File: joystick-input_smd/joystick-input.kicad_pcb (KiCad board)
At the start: 2 copper layers, 53.3 x 38.6 mm, 16 parts, among them J1 Conn_01x18_Male, J2 Conn_01x14_Male, J3 Conn_01x14_Male

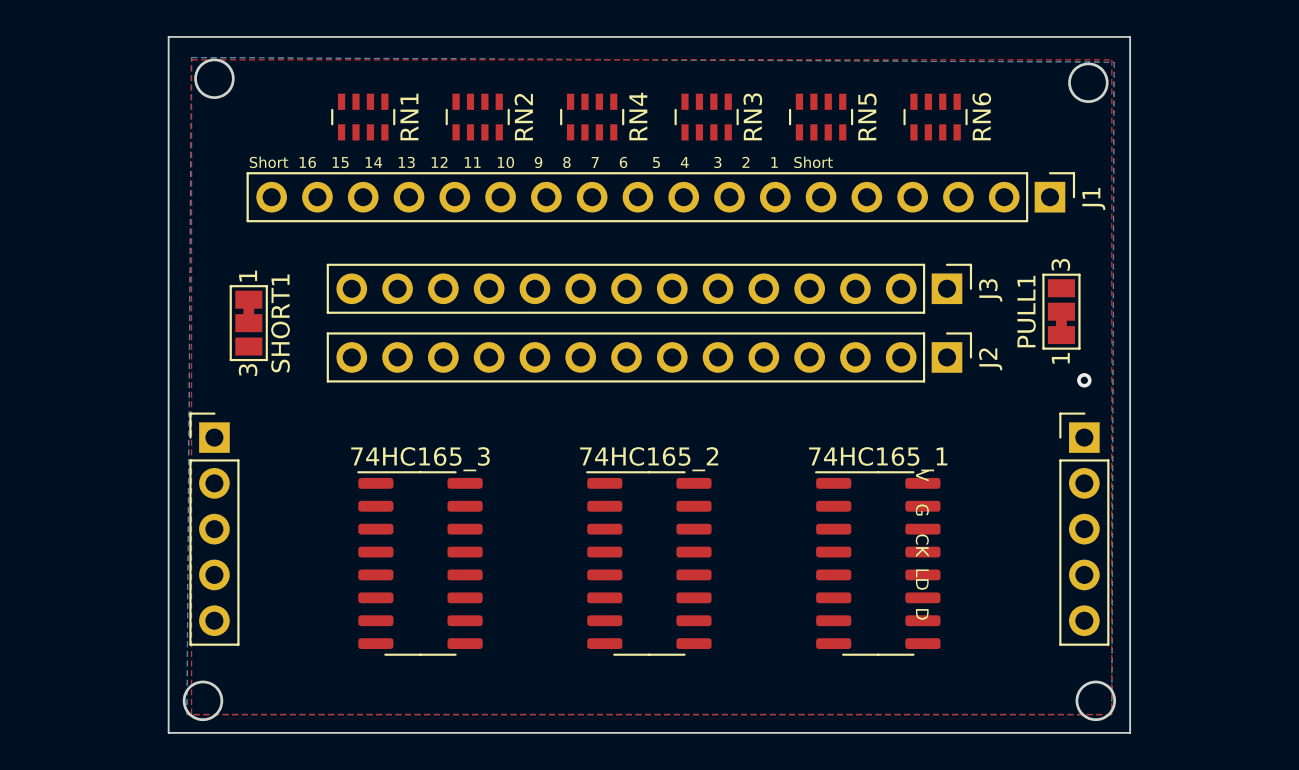
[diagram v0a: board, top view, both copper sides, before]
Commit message: am_joyin SMD 보드 레이아웃 변경
Signed-off-by: Ju, Gyeong-min <jcmh74@gmail.com>
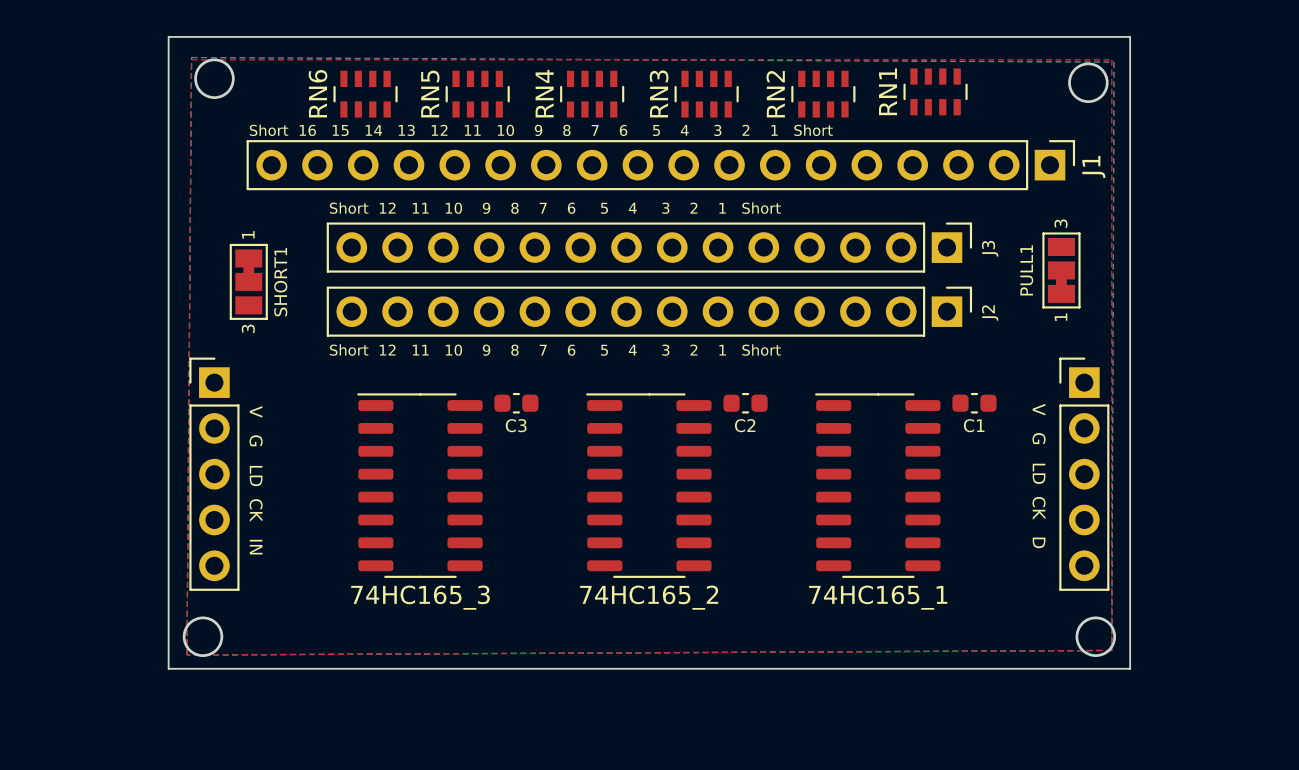
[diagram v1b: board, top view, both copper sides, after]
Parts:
- added C1: C, Capacitor_SMD:C_0603_1608Metric, F.Cu at (156.5, 82.5)
- added C2: C, Capacitor_SMD:C_0603_1608Metric, F.Cu at (143.8, 82.5)
- added C3: C, Capacitor_SMD:C_0603_1608Metric, F.Cu at (131.1, 82.5)
- moved RN1 31.8 mm to (154.3, 65.3), turned to 90 degrees
- moved RN6 31.6 mm to (122.7, 65.4), turned to 90 degrees
- moved RN2 19.2 mm to (148.1, 65.4), turned to 90 degrees
- moved RN5 19.1 mm to (128.9, 65.4), turned to 90 degrees
- moved 74HC165_1 4.32 mm to (151.1, 87.1)
- moved 74HC165_2 4.32 mm to (138.4, 87.1)
- moved 74HC165_3 4.32 mm to (125.7, 87.1)
- moved IN1 3.05 mm to (114.3, 81.4)
- moved OUT1 3.05 mm to (162.6, 81.4)
- moved J2 2.54 mm to (154.9, 77.5)
- moved J3 2.29 mm to (154.9, 73.9)
- moved PULL1 2.29 mm to (161.3, 75.2)
- moved SHORT1 2.29 mm to (116.2, 75.8)
- moved J1 1.78 mm to (160.7, 69.3)
- moved RN3 1.27 mm to (141.6, 65.4), turned to 90 degrees
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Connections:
- IN1 pad 3: /CLK -> /LOAD
- IN1 pad 4: /LOAD -> /CLK
- OUT1 pad 3: /CLK -> /LOAD
- OUT1 pad 4: /LOAD -> /CLK
- RN1 pad 1: /C_UP -> /C_R2
- RN1 pad 2: /C_DOWN -> /C_L2
- RN1 pad 3: /C_LEFT -> /C_Y2
- RN1 pad 4: /C_RIGHT -> /C_X2
- RN2 pad 1: /C_EX1 -> /C_EX4
- RN2 pad 2: /C_EX2 -> /C_EX3
- RN2 pad 3: /C_EX3 -> /C_EX2
- RN2 pad 4: /C_EX4 -> /C_EX1
- RN3 pad 1: /C_START2 -> /C_B2
- RN3 pad 2: /C_SELECT2 -> /C_A2
- RN3 pad 3: /C_A2 -> /C_SELECT2
- RN3 pad 4: /C_B2 -> /C_START2
- RN4 pad 1: /C_X2 -> /C_RIGHT
- RN4 pad 2: /C_Y2 -> /C_LEFT
- RN4 pad 3: /C_L2 -> /C_DOWN
- RN4 pad 4: /C_R2 -> /C_UP
- RN5 pad 1: /C_START -> /C_B
- RN5 pad 2: /C_SELECT -> /C_A
- RN5 pad 3: /C_A -> /C_SELECT
- RN5 pad 4: /C_B -> /C_START
- RN6 pad 1: /C_X -> /C_R
- RN6 pad 2: /C_Y -> /C_L
- RN6 pad 3: /C_L -> /C_Y
- RN6 pad 4: /C_R -> /C_X
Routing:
- net GND: vias 1 -> 0
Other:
- board size 53.3 x 38.6 mm -> 53.3 x 35.1 mm
- board text added: "Short 12 11 10 9 8 7 6 5 4 3 2 1 Short"
- board text added: "V G LD CK D"
- board text added: "V G LD CK IN"
- board text removed: "V G CK LD D"

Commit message: joystick smd 타입 74hc165 갯수를 4개로 늘림
Signed-off-by: Ju, Gyeong-min <jcmh74@gmail.com>
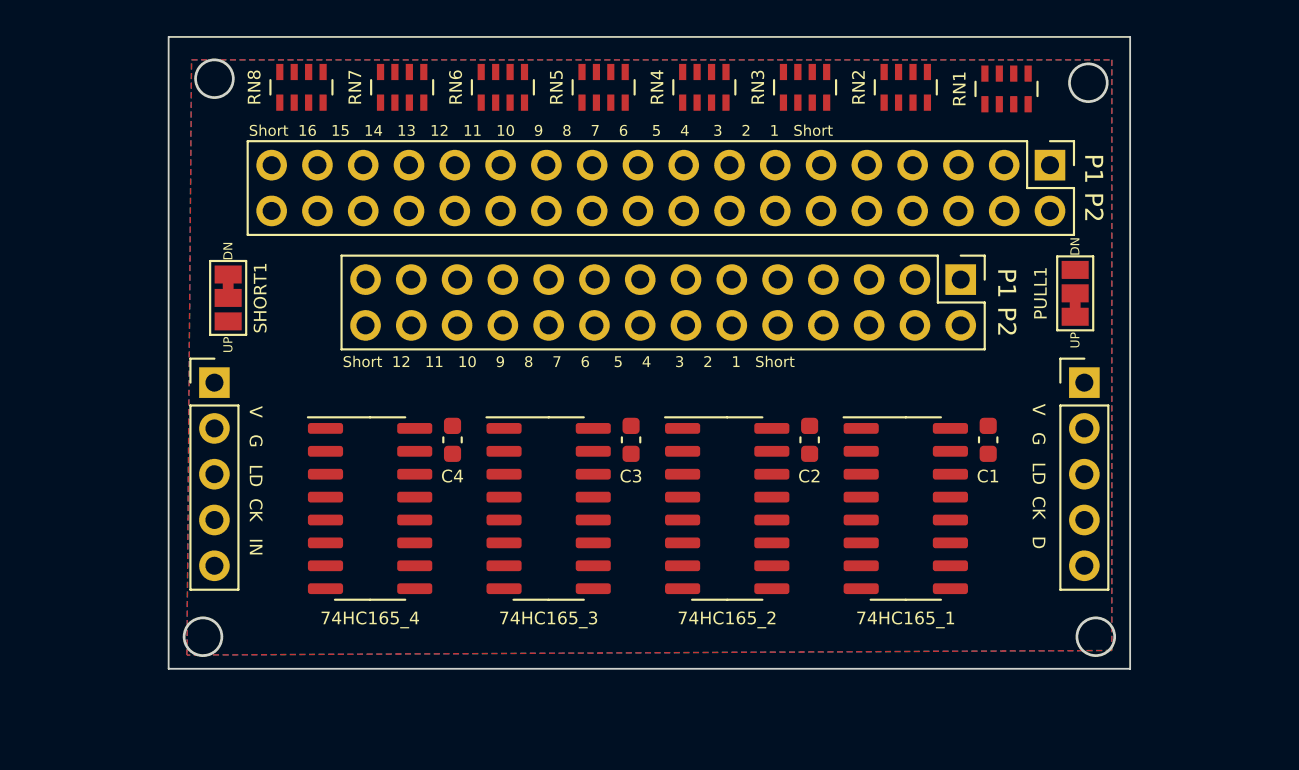
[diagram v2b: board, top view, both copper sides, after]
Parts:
- removed J3: Conn_01x14_Male, Connector_PinHeader_2.54mm:PinHeader_1x14_P2.54mm_Vertical
- added 74HC165_4: 74HC165, Package_SO:SOIC-16_3.9x9.9mm_P1.27mm, F.Cu at (122.9, 88.4)
- added C4: C, Capacitor_SMD:C_0603_1608Metric, F.Cu at (127.5, 84.6)
- added RN1: R_Pack04, Resistor_SMD:R_Array_Concave_4x0603, F.Cu at (158.2, 65.1)
- added RN2: R_Pack04, Resistor_SMD:R_Array_Concave_4x0603, F.Cu at (152.7, 65.0)
- J1: value Conn_01x18_Male -> Conn_02x18_Odd_Even; footprint Connector_PinHeader_2.54mm:PinHeader_1x18_P2.54mm_Vertical -> Connector_PinHeader_2.54mm:PinHeader_2x18_P2.54mm_Vertical
- J2: value Conn_01x14_Male -> Conn_02x14_Odd_Even; footprint Connector_PinHeader_2.54mm:PinHeader_1x14_P2.54mm_Vertical -> Connector_PinHeader_2.54mm:PinHeader_2x14_P2.54mm_Vertical
- moved RN8 35.2 mm to (119.1, 65.0)
- moved RN3 24.4 mm to (147.1, 65.0)
- moved RN7 23.4 mm to (124.7, 65.0)
- moved RN4 12.6 mm to (141.5, 65.0)
- moved RN6 11.3 mm to (130.3, 65.0)
- moved 74HC165_3 7.22 mm to (132.8, 88.4)
- moved C3 6.68 mm to (137.4, 84.6), turned to 270 degrees
- moved 74HC165_2 4.50 mm to (142.7, 88.4)
- moved C2 4.10 mm to (147.3, 84.6), turned to 270 degrees
- moved C1 2.17 mm to (157.2, 84.6), turned to 270 degrees
- moved 74HC165_1 1.98 mm to (152.7, 88.4)
- moved J2 1.93 mm to (155.7, 75.7)
- moved PULL1 1.48 mm to (162.1, 76.5)
- moved SHORT1 1.45 mm to (115.1, 76.7)
- moved RN5 0.74 mm to (135.9, 65.0)
- renumbered RN6 to RN3, RN5 to RN4, RN4 to RN5, RN3 to RN6, RN2 to RN7, RN1 to RN8
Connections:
- 74HC165_1 pad 11: /C_B -> /C_P1_B
- 74HC165_1 pad 12: /C_A -> /C_P1_A
- 74HC165_1 pad 13: /C_SELECT -> /C_P1_SELECT
- 74HC165_1 pad 14: /C_START -> /C_P1_START
- 74HC165_1 pad 3: /C_RIGHT -> /C_P1_RIGHT
- 74HC165_1 pad 4: /C_LEFT -> /C_P1_LEFT
- 74HC165_1 pad 5: /C_DOWN -> /C_P1_DOWN
- 74HC165_1 pad 6: /C_UP -> /C_P1_UP
- 74HC165_2 pad 11: /C_EX4 -> /C_P1_EX3
- 74HC165_2 pad 12: /C_EX3 -> /C_P1_EX2
- 74HC165_2 pad 13: /C_EX2 -> /C_P1_EX1
- 74HC165_2 pad 14: /C_EX1 -> /C_P1_HK
- 74HC165_2 pad 3: /C_R -> /C_P1_R
- 74HC165_2 pad 4: /C_L -> /C_P1_L
- 74HC165_2 pad 5: /C_Y -> /C_P1_Y
- 74HC165_2 pad 6: /C_X -> /C_P1_X
- 74HC165_3 pad 10: /D_IN -> /Q7_3
- 74HC165_3 pad 11: /C_R2 -> /C_P2_B
- 74HC165_3 pad 12: /C_L2 -> /C_P2_A
- 74HC165_3 pad 13: /C_Y2 -> /C_P2_SELECT
- 74HC165_3 pad 14: /C_X2 -> /C_P2_START
- 74HC165_3 pad 3: /C_B2 -> /C_P2_RIGHT
- 74HC165_3 pad 4: /C_A2 -> /C_P2_LEFT
- 74HC165_3 pad 5: /C_SELECT2 -> /C_P2_DOWN
- 74HC165_3 pad 6: /C_START2 -> /C_P2_UP
- J1 pad 10: /C_X -> /C_P2_RIGHT
- J1 pad 11: /C_Y -> /C_P1_START
- J1 pad 12: /C_L -> /C_P2_START
- J1 pad 13: /C_R -> /C_P1_SELECT
- J1 pad 14: /C_EX1 -> /C_P2_SELECT
- J1 pad 15: /C_EX2 -> /C_P1_A
- J1 pad 16: /C_EX3 -> /C_P2_A
- J1 pad 17: /C_EX4 -> /C_P1_B
- J1 pad 18: /C_SHORT -> /C_P2_B
- J1 pad 2: /C_UP -> /C_SHORT
- J1 pad 3: /C_DOWN -> /C_P1_UP
- J1 pad 4: /C_LEFT -> /C_P2_UP
- J1 pad 5: /C_RIGHT -> /C_P1_DOWN
- J1 pad 6: /C_START -> /C_P2_DOWN
- J1 pad 7: /C_SELECT -> /C_P1_LEFT
- J1 pad 8: /C_A -> /C_P2_LEFT
- J1 pad 9: /C_B -> /C_P1_RIGHT
- J2 pad 10: /C_X -> /C_P1_EX3
- J2 pad 11: /C_Y -> /C_P1_START
- J2 pad 12: /C_L -> /C_P2_UP
- J2 pad 13: /C_R -> /C_P1_SELECT
- J2 pad 14: /C_SHORT -> /C_P2_DOWN
- J2 pad 2: /C_UP -> /C_SHORT
- J2 pad 3: /C_DOWN -> /C_P1_UP
- J2 pad 4: /C_LEFT -> /C_P1_HK
- J2 pad 5: /C_RIGHT -> /C_P1_DOWN
- J2 pad 6: /C_START -> /C_P1_EX1
- J2 pad 7: /C_SELECT -> /C_P1_LEFT
- J2 pad 8: /C_A -> /C_P1_EX2
- J2 pad 9: /C_B -> /C_P1_RIGHT
- RN3 pad 1: /C_R -> /C_P1_R
- RN3 pad 2: /C_L -> /C_P1_L
- RN3 pad 3: /C_Y -> /C_P1_Y
- RN3 pad 4: /C_X -> /C_P1_X
- RN4 pad 1: /C_B -> /C_P1_EX3
- RN4 pad 2: /C_A -> /C_P1_EX2
- RN4 pad 3: /C_SELECT -> /C_P1_EX1
- RN4 pad 4: /C_START -> /C_P1_HK
- RN5 pad 1: /C_RIGHT -> /C_P2_RIGHT
- RN5 pad 2: /C_LEFT -> /C_P2_LEFT
- RN5 pad 3: /C_DOWN -> /C_P2_DOWN
- RN5 pad 4: /C_UP -> /C_P2_UP
- RN6 pad 1: /C_B2 -> /C_P2_B
- RN6 pad 2: /C_A2 -> /C_P2_A
- RN6 pad 3: /C_SELECT2 -> /C_P2_SELECT
- RN6 pad 4: /C_START2 -> /C_P2_START
- RN7 pad 1: /C_EX4 -> /C_P2_R
- RN7 pad 2: /C_EX3 -> /C_P2_L
- RN7 pad 3: /C_EX2 -> /C_P2_Y
- RN7 pad 4: /C_EX1 -> /C_P2_X
- RN8 pad 1: /C_R2 -> /C_P2_EX3
- RN8 pad 2: /C_L2 -> /C_P2_EX2
- RN8 pad 3: /C_Y2 -> /C_P2_EX1
- RN8 pad 4: /C_X2 -> /C_P2_HK
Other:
- board text added: "P1 P2"

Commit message: joystick smd 레이아웃 변경
Signed-off-by: Ju, Gyeong-min <jcmh74@gmail.com>
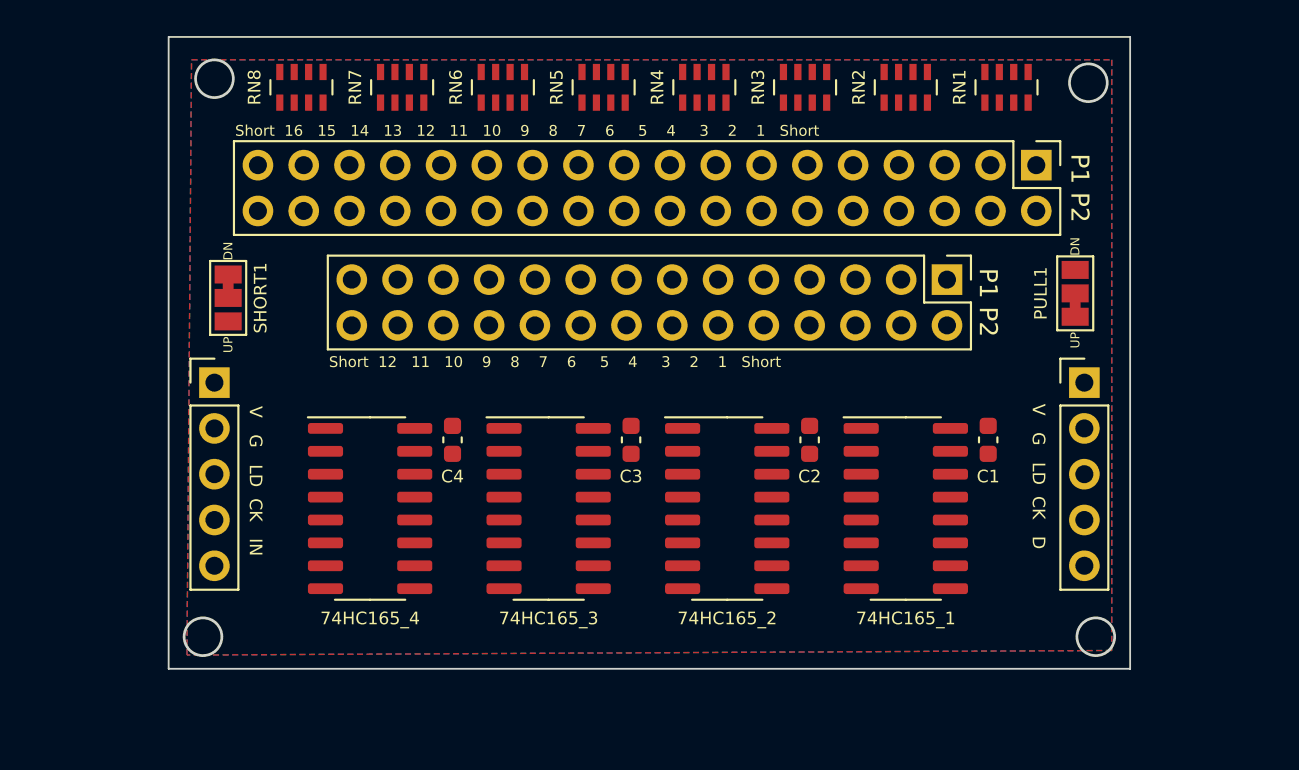
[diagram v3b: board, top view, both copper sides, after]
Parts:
- moved J1 0.76 mm to (159.9, 69.3)
- moved J2 0.76 mm to (154.9, 75.7)
- moved RN1 0.09 mm to (158.2, 65.0)

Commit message: 조이스틱 입력보드 smd 버전 1차 완성
Signed-off-by: Ju, Gyeong-min <jcmh74@gmail.com>
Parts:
- removed 74HC165_4: 74HC165, Package_SO:SOIC-16_3.9x9.9mm_P1.27mm
- removed C4: C, Capacitor_SMD:C_0603_1608Metric
- removed RN7, RN8: R_Pack04, Resistor_SMD:R_Array_Concave_4x0603
- IN1: footprint Connector_PinHeader_2.54mm:PinHeader_1x05_P2.54mm_Vertical -> Connector_PinSocket_2.54mm:PinSocket_1x05_P2.54mm_Horizontal
- J1: value Conn_02x18_Odd_Even -> Conn_01x18; footprint Connector_PinHeader_2.54mm:PinHeader_2x18_P2.54mm_Vertical -> Connector_PinHeader_2.54mm:PinHeader_1x18_P2.54mm_Vertical
- OUT1: footprint Connector_PinHeader_2.54mm:PinHeader_1x05_P2.54mm_Vertical -> Connector_PinHeader_2.54mm:PinHeader_1x05_P2.54mm_Horizontal
- moved RN5 29.3 mm to (119.4, 89.3), turned to 0 degrees
- moved RN3 27.1 mm to (132.6, 87.9), turned to 0 degrees
- moved RN4 26.9 mm to (144.7, 91.7), turned to 180 degrees
- moved RN6 26.7 mm to (131.1, 91.7), turned to 180 degrees
- moved RN1 26.0 mm to (145.8, 87.9), turned to 0 degrees
- moved RN2 24.7 mm to (157.2, 89.3), turned to 180 degrees
- moved J1 8.64 mm to (159.9, 78.0)
- moved 74HC165_3 7.92 mm to (125.0, 89.3)
- moved C3 6.94 mm to (130.5, 84.3), turned to 0 degrees
- moved 74HC165_2 4.30 mm to (138.5, 89.3)
- moved J2 4.19 mm to (154.8, 71.5)
- moved C2 3.56 mm to (143.8, 84.5), turned to 0 degrees
- moved SHORT1 2.07 mm to (115.4, 74.7), turned to 180 degrees
- moved PULL1 1.89 mm to (161.4, 74.7), turned to 180 degrees
- moved 74HC165_1 1.33 mm to (151.6, 89.2)
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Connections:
- 74HC165_2 pad 11: /C_P1_EX3 -> /C_P2_RIGHT
- 74HC165_2 pad 12: /C_P1_EX2 -> /C_P2_LEFT
- 74HC165_2 pad 13: /C_P1_EX1 -> /C_P2_DOWN
- 74HC165_2 pad 14: /C_P1_HK -> /C_P2_UP
- 74HC165_3 pad 10: /Q7_3 -> /D_IN
- 74HC165_3 pad 11: /C_P2_B -> /C_P2_R
- 74HC165_3 pad 12: /C_P2_A -> /C_P2_L
- 74HC165_3 pad 13: /C_P2_SELECT -> /C_P2_Y
- 74HC165_3 pad 14: /C_P2_START -> /C_P2_X
- 74HC165_3 pad 3: /C_P2_RIGHT -> /C_P2_B
- 74HC165_3 pad 4: /C_P2_LEFT -> /C_P2_A
- 74HC165_3 pad 5: /C_P2_DOWN -> /C_P2_SELECT
- 74HC165_3 pad 6: /C_P2_UP -> /C_P2_START
- J1 pad 10: /C_P2_RIGHT -> /C_P1_X
- J1 pad 11: /C_P1_START -> /C_P1_Y
- J1 pad 12: /C_P2_START -> /C_P1_L
- J1 pad 13: /C_P1_SELECT -> /C_P1_R
- J1 pad 14: /C_P2_SELECT -> /C_P2_UP
- J1 pad 15: /C_P1_A -> /C_P2_DOWN
- J1 pad 16: /C_P2_A -> /C_P2_LEFT
- J1 pad 17: /C_P1_B -> /C_P2_RIGHT
- J1 pad 18: /C_P2_B -> /C_SHORT
- J1 pad 2: /C_SHORT -> /C_P1_UP
- J1 pad 3: /C_P1_UP -> /C_P1_DOWN
- J1 pad 4: /C_P2_UP -> /C_P1_LEFT
- J1 pad 5: /C_P1_DOWN -> /C_P1_RIGHT
- J1 pad 6: /C_P2_DOWN -> /C_P1_START
- J1 pad 7: /C_P1_LEFT -> /C_P1_SELECT
- J1 pad 8: /C_P2_LEFT -> /C_P1_A
- J1 pad 9: /C_P1_RIGHT -> /C_P1_B
- J2 pad 10: /C_P1_EX3 -> /C_P2_RIGHT
- J2 pad 12: /C_P2_UP -> /C_P2_START
- J2 pad 14: /C_P2_DOWN -> /C_P2_SELECT
- J2 pad 16: /C_P2_LEFT -> /C_P2_A
- J2 pad 18: /C_P2_RIGHT -> /C_P2_B
- J2 pad 20: /C_P2_START -> /C_P2_X
- J2 pad 22: /C_P2_SELECT -> /C_P2_Y
- J2 pad 24: /C_P2_A -> /C_P2_L
- J2 pad 26: /C_P2_B -> /C_P2_R
- J2 pad 4: /C_P1_HK -> /C_P2_UP
- J2 pad 6: /C_P1_EX1 -> /C_P2_DOWN
- J2 pad 8: /C_P1_EX2 -> /C_P2_LEFT
- RN1 pad 1: /C_P1_RIGHT -> /PULL
- RN1 pad 2: /C_P1_LEFT -> /PULL
- RN1 pad 3: /C_P1_DOWN -> /PULL
- RN1 pad 4: /C_P1_UP -> /PULL
- RN1 pad 5: /PULL -> /C_P1_UP
- RN1 pad 6: /PULL -> /C_P1_DOWN
- RN1 pad 7: /PULL -> /C_P1_LEFT
- RN1 pad 8: /PULL -> /C_P1_RIGHT
- RN2 pad 1: /C_P1_B -> /PULL
- RN2 pad 2: /C_P1_A -> /PULL
- RN2 pad 3: /C_P1_SELECT -> /PULL
- RN2 pad 4: /C_P1_START -> /PULL
- RN2 pad 5: /PULL -> /C_P1_START
- RN2 pad 6: /PULL -> /C_P1_SELECT
- RN2 pad 7: /PULL -> /C_P1_A
- RN2 pad 8: /PULL -> /C_P1_B
- RN3 pad 1: /C_P1_R -> /PULL
- RN3 pad 2: /C_P1_L -> /PULL
- RN3 pad 3: /C_P1_Y -> /PULL
- RN3 pad 4: /C_P1_X -> /PULL
- RN3 pad 5: /PULL -> /C_P1_X
- RN3 pad 6: /PULL -> /C_P1_Y
- RN3 pad 7: /PULL -> /C_P1_L
- RN3 pad 8: /PULL -> /C_P1_R
- RN4 pad 1: /C_P1_EX3 -> /PULL
- RN4 pad 2: /C_P1_EX2 -> /PULL
- RN4 pad 3: /C_P1_EX1 -> /PULL
- RN4 pad 4: /C_P1_HK -> /PULL
- RN4 pad 5: /PULL -> /C_P2_UP
- RN4 pad 6: /PULL -> /C_P2_DOWN
- RN4 pad 7: /PULL -> /C_P2_LEFT
- RN4 pad 8: /PULL -> /C_P2_RIGHT
- RN5 pad 1: /C_P2_RIGHT -> /PULL
- RN5 pad 2: /C_P2_LEFT -> /PULL
- RN5 pad 3: /C_P2_DOWN -> /PULL
- RN5 pad 4: /C_P2_UP -> /PULL
- RN5 pad 5: /PULL -> /C_P2_START
- RN5 pad 6: /PULL -> /C_P2_SELECT
- RN5 pad 7: /PULL -> /C_P2_A
- RN5 pad 8: /PULL -> /C_P2_B
- RN6 pad 1: /C_P2_B -> /PULL
- RN6 pad 2: /C_P2_A -> /PULL
- RN6 pad 3: /C_P2_SELECT -> /PULL
- RN6 pad 4: /C_P2_START -> /PULL
- RN6 pad 5: /PULL -> /C_P2_X
- RN6 pad 6: /PULL -> /C_P2_Y
- RN6 pad 7: /PULL -> /C_P2_L
- RN6 pad 8: /PULL -> /C_P2_R
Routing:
- net /PULL: track 0.00 -> 99.9 mm, vias 0 -> 5
- net VCC: track 0.00 -> 75.3 mm
- net /C_SHORT: track 0.00 -> 72.1 mm, vias 0 -> 1
- net /C_P2_RIGHT: track 0.00 -> 62.4 mm, vias 0 -> 1
- net /C_P2_START: track 0.00 -> 60.0 mm, vias 0 -> 1
- net /C_P2_LEFT: track 0.00 -> 59.7 mm, vias 0 -> 1
- net /C_P2_DOWN: track 0.00 -> 56.9 mm, vias 0 -> 1
- net /CLK: track 0.00 -> 55.1 mm
- net /C_P2_SELECT: track 0.00 -> 54.6 mm, vias 0 -> 1
- net /LOAD: track 0.00 -> 53.2 mm
- net /C_P2_UP: track 0.00 -> 52.6 mm, vias 0 -> 1
- net /C_P2_A: track 0.00 -> 49.6 mm, vias 0 -> 1
- net /C_P2_X: track 0.00 -> 45.4 mm, vias 0 -> 2
- net /C_P2_Y: track 0.00 -> 41.3 mm, vias 0 -> 2
- net /C_P2_B: track 0.00 -> 37.2 mm, vias 0 -> 1
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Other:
- board size 53.3 x 35.1 mm -> 53.3 x 29 mm
- board text added: "DT CK LD G V"
- board text removed: "V G LD CK D"
